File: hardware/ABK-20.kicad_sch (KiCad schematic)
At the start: 52 parts, among them J1 CONN_01X04, J2 CONN_01X04, J3 CONN_02X03, J4 Con_3-5V, J5 USB_C_6P, J6 Sync_Jumper, SW1 SW_SPST, SW2 SW_Push, SW3 SW_SPDT_MSM, SW4 SW_Push, U1 ATTINY85-20SU, U2 PAM8002, U3 7805

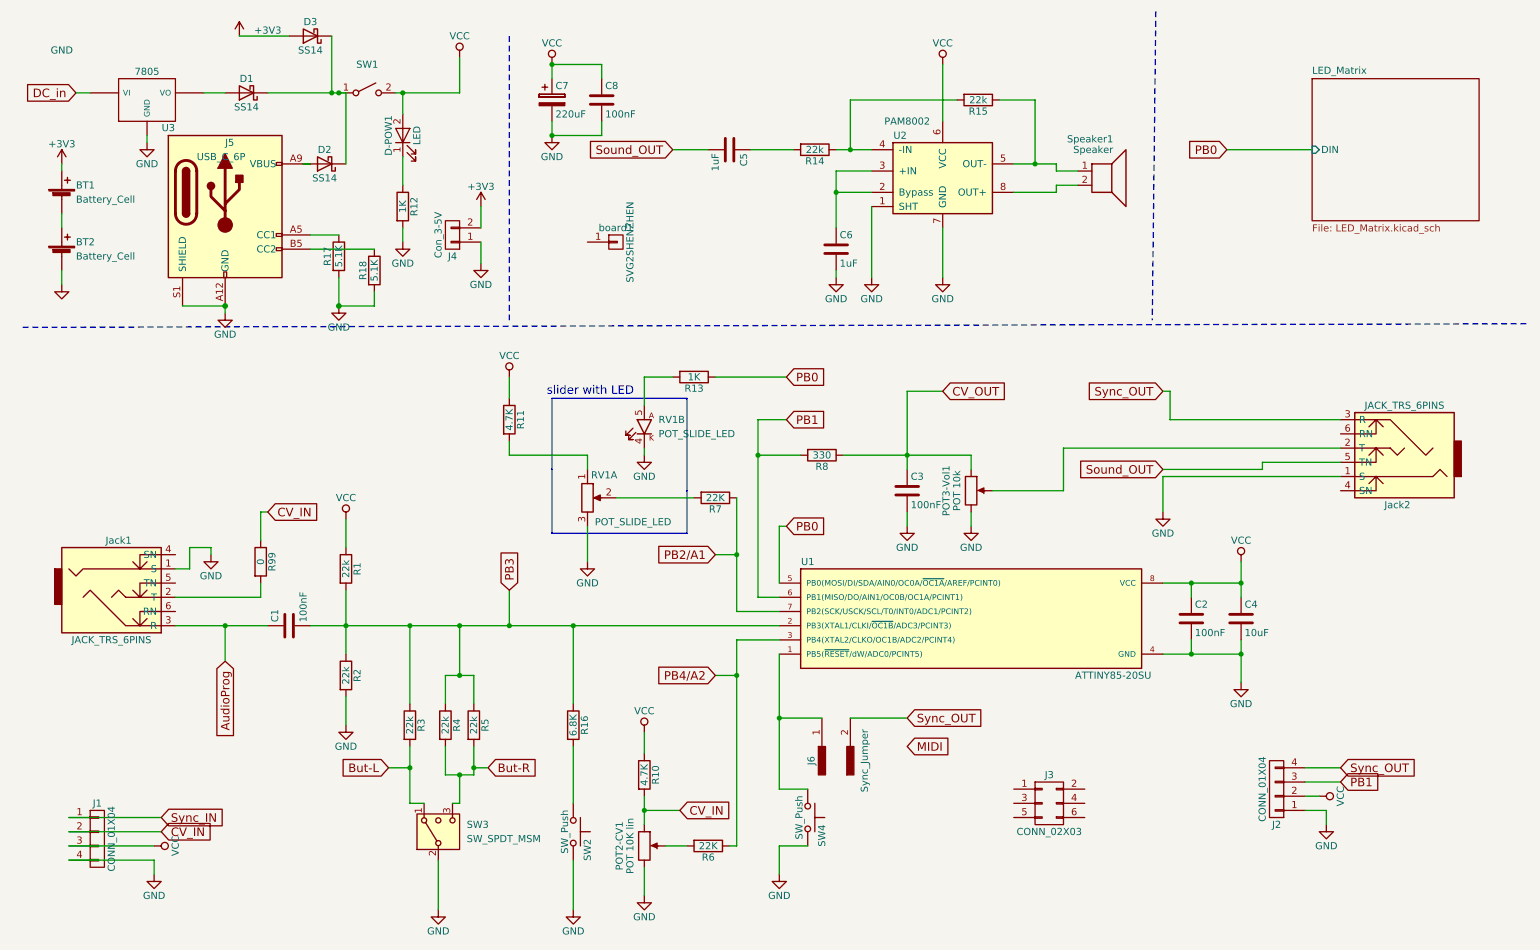
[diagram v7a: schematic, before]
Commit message: fix(3d-models): update all 3D model paths to KiCad 9 and bundle project 3D models
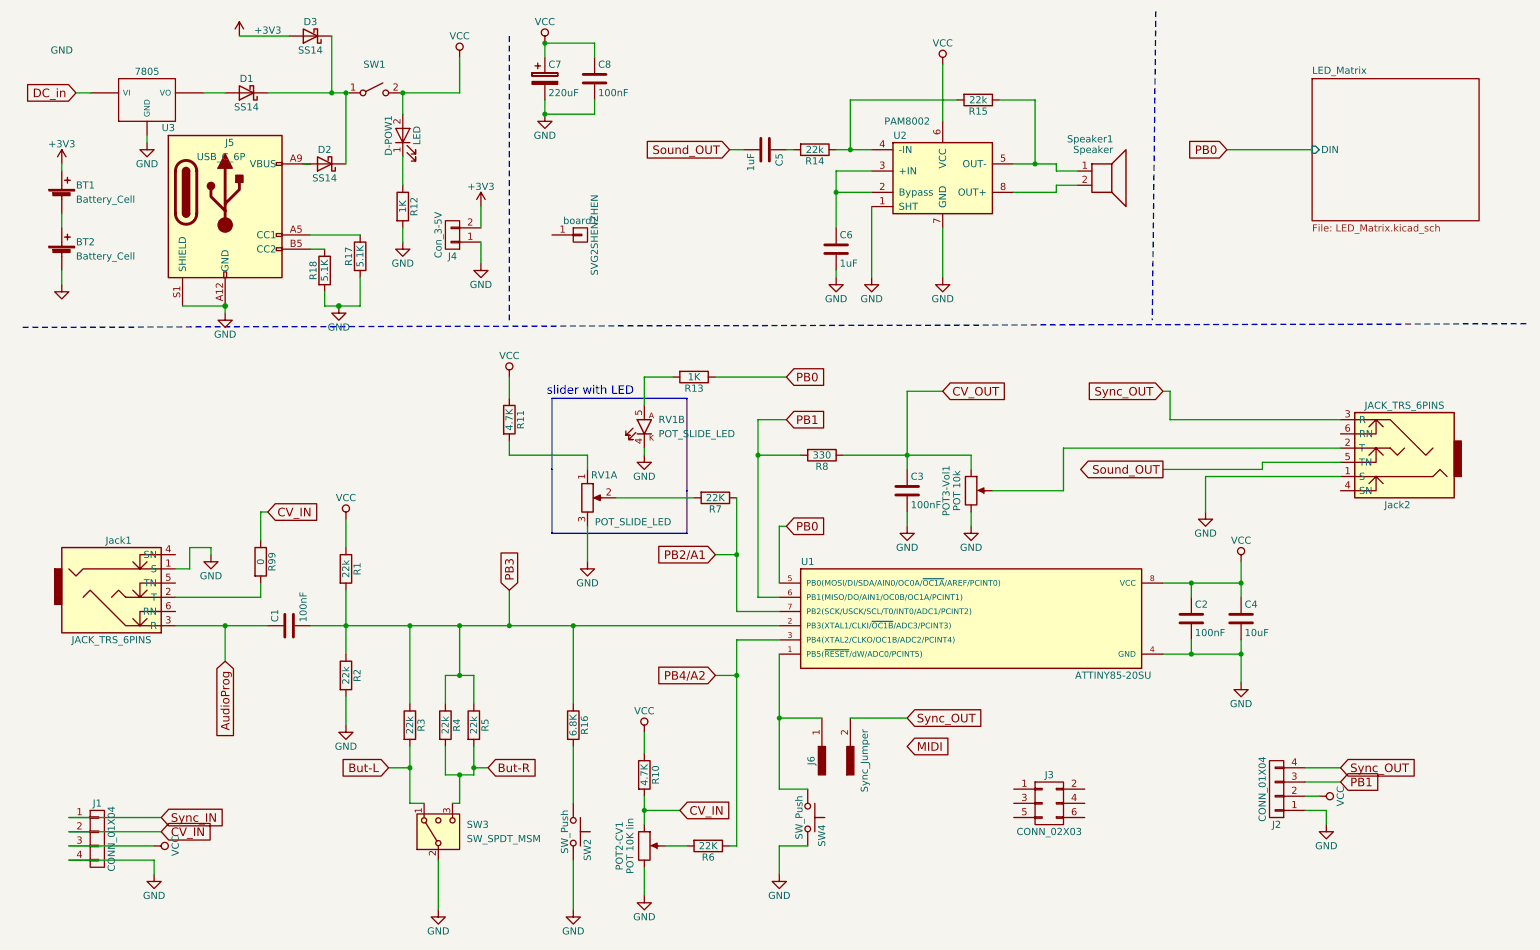
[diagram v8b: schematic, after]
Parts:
- RV1: footprint 8Bitmixtape_reworked:Potentiometer_Bourns_PTL30_Single_Slide_LED -> 8Bitmixtape_reworked:Potentiometer_Bourns_PTL20_Single_Slide_LED
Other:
- moved on the sheet: C5, C7, C8, R17, R18, SW1, board1
